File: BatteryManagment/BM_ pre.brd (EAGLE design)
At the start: 107.7 x 100 mm, 98 parts, among them IC1 LMV321M5, U1 ATMEGA328P-AU, U2 LTC4440EMS8E-5PBF

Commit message: Schematic PDF uplaod
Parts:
- moved MOTOR+ 2.20 mm to (98.3, 19.1)
- moved PAD1 1.48 mm to (35.2, 94.9)
- moved PAD2 1.47 mm to (41.4, 94.8)
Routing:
- net GND: track 58.0 -> 129.5 mm, vias 0 -> 13
- net BATTERY+: track 89.5 -> 107.1 mm
- net CHARGE_PWM: track 69.2 -> 62.3 mm
- net N$20: track 66.9 -> 65.4 mm
- net MOTOR+: track 38.3 -> 37.2 mm
- added copper zone on layer 1, net GND

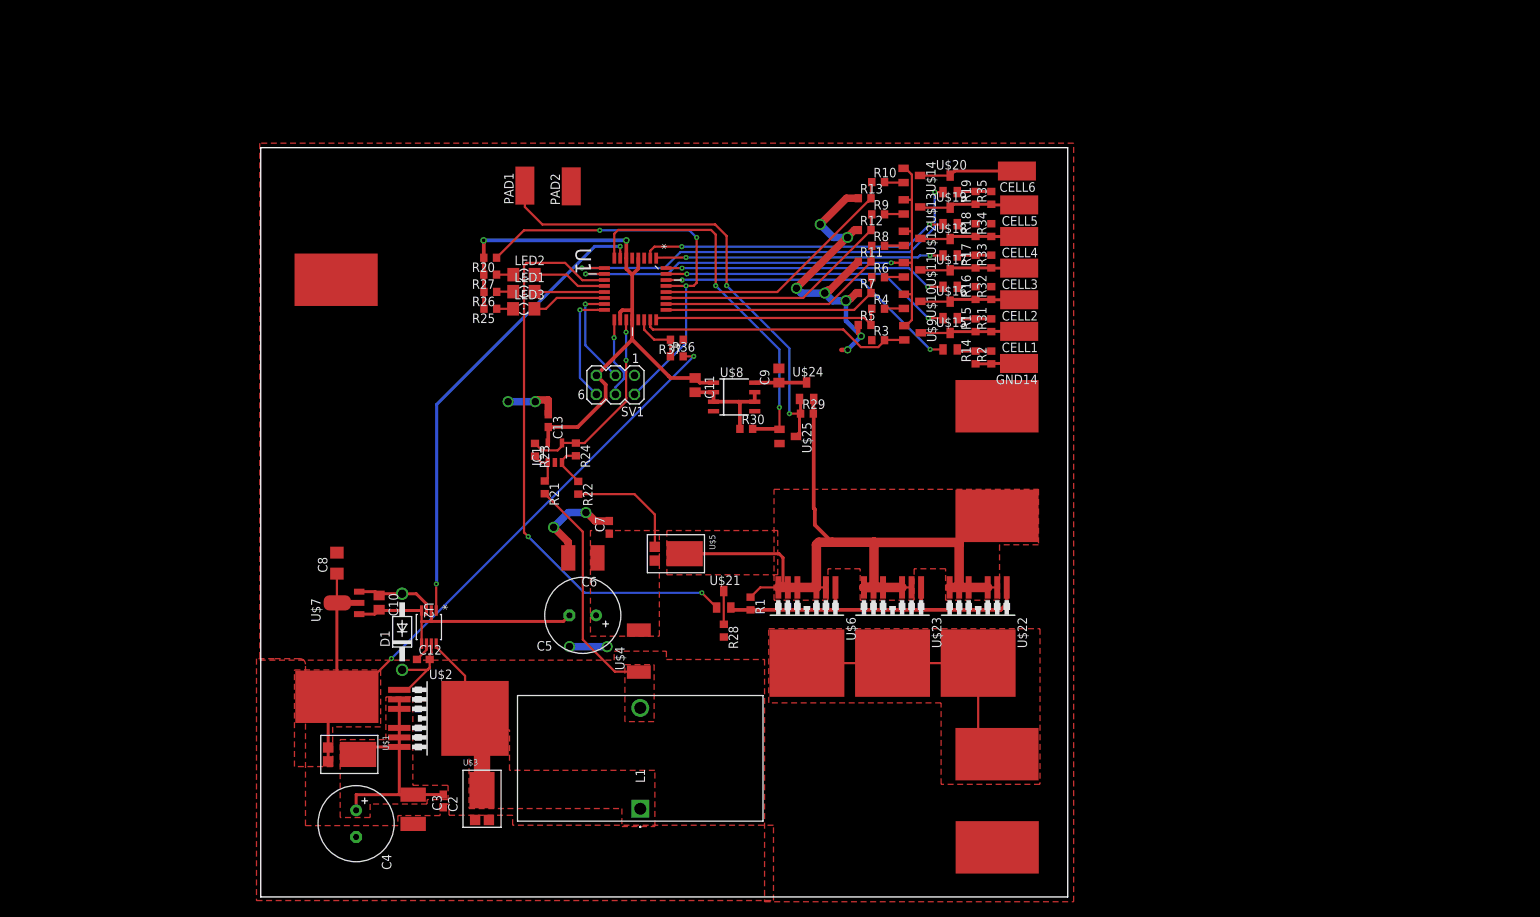
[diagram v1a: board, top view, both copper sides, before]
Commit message: just for fun.... nooot
changed some parts
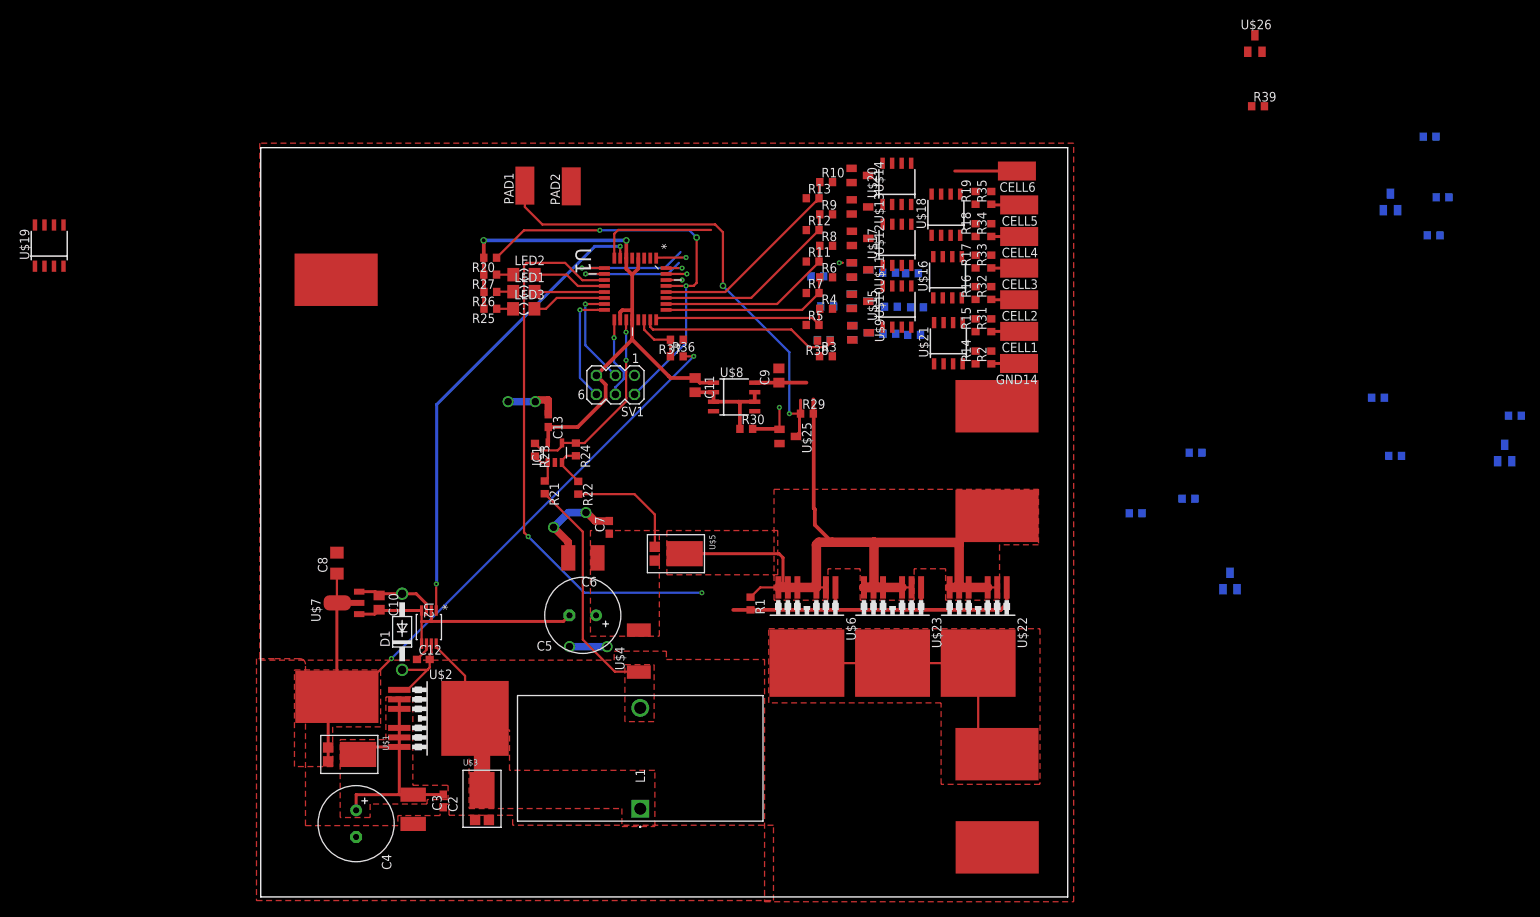
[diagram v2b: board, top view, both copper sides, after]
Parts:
- added R38, R39, R40, R41, R42, R43, R44, R45, R46, R47, R48, R49, R50, R51, R52, R53, R54, R55, R56: (no value), rcl:R0603
- added U$26, U$27, U$28, U$29, U$30, U$31: BC817, BM_pre:SOT23
- U$15, U$16, U$17, U$18, U$19, U$20, U$21: value BC817 -> IRF9310PBF; device BM_pre:SOT23 -> BM_pre:SOIC8
- U$24: value FDN306P -> BC817
- moved U$19 120.3 mm to (-28.2, 86.9)
- moved R28 46.9 mm to (87.2, 75.0), flipped to the bottom, turned to 180 degrees
- moved U$21 45.5 mm to (91.8, 73.9)
- moved U$24 10.6 mm to (80.1, 75.3), flipped to the bottom, turned to 90 degrees
- moved U$15 8.46 mm to (84.9, 78.8)
- moved U$17 8.40 mm to (84.9, 87.0)
- moved R3 7.29 mm to (75.4, 72.2)
- moved U$20 7.11 mm to (84.9, 95.2)
- moved R10 6.94 mm to (75.5, 95.4)
- moved R4 6.94 mm to (75.5, 78.5)
- moved R6 6.94 mm to (75.5, 82.7)
- moved R8 6.94 mm to (75.5, 86.9)
- moved R9 6.94 mm to (75.5, 91.1)
- moved U$10 6.94 mm to (80.0, 79.5)
- moved U$11 6.94 mm to (80.0, 83.7)
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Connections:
- new net N$21: U$10.2, U$11.2, U$12.2, U$13.2, U$14.2, U$9.2
- new net N$22: R28.1, R45.2, U$21.4
- new net N$28: R40.1, R46.2, U$15.4
- new net N$29: R41.1, R47.2, U$16.4
- new net N$3: R13.1, U$14.3
- new net N$30: R42.1, R48.2, U$17.4
- new net N$31: R43.1, R49.2, U$18.4
- new net N$32: R44.1, R50.2, U$20.4
- new net N$33: R49.1, U$28.3
- new net N$34: R50.1, U$31.3
- new net N$35: R48.1, U$29.3
- new net N$36: R47.1, U$27.3
- new net N$37: R46.1, U$30.3
- new net N$38: R45.1, U$24.3
- new net N$39: R51.2, U$31.1
- new net N$40: R52.2, U$28.1
- new net N$41: R53.2, U$29.1
- new net N$42: R54.2, U$27.1
- new net N$43: R55.2, U$30.1
- new net N$44: R56.2, U$24.1
- net ADC_BAT_1: now also R38.1; no longer U$9.2
- net BATTERY+: now also U$19.1, U$19.2, U$19.3; no longer U$24.2
- net C1_B: now also R56.1; no longer U$15.1
- net C2_B: now also R55.1; no longer U$16.1
- net C3_B: now also R54.1; no longer U$17.1
- net C4_B: now also R53.1; no longer U$18.1
- net C5_B: now also R52.1; no longer U$19.1
- net C6_B: now also R51.1; no longer U$20.1
- net CELL1: now also R28.2, R38.2, U$21.5, U$21.6, U$21.7, U$21.8; no longer U$15.3, U$9.3
- net CELL2: now also R16.2, R32.2, R4.2, R40.2, U$15.5, U$15.6, U$15.7, U$15.8; no longer R16.1, R32.1, U$10.3, U$16.3
- net CELL3: now also R17.2, R33.2, R41.2, R6.2, U$16.5, U$16.6, U$16.7, U$16.8; no longer R17.1, R33.1, U$11.3, U$17.3
- net CELL4: now also R18.2, R34.2, R42.2, R8.2, U$17.5, U$17.6, U$17.7, U$17.8; no longer R18.1, R34.1, U$12.3, U$18.3
- net CELL5: now also R19.2, R35.2, R43.2, R9.2, U$18.5, U$18.6, U$18.7, U$18.8; no longer R19.1, R35.1, U$13.3, U$19.3
- net CELL6: now also R10.2, R44.2, U$20.5, U$20.6, U$20.7, U$20.8; no longer U$14.3, U$20.3
- net CHARGE_CONTROL: now also U$26.1
- net GND: now also R39.2, U$24.2, U$27.2, U$28.2, U$29.2, U$30.2, U$31.2; no longer R11.1, R12.1, R13.1, R28.2, R3.1, R5.1, R7.1
- net MOTOR_CONTROL: now also U$26.3; no longer U$21.2
- net N$10: now also R3.1, U$9.3; no longer R10.2, U$14.2
- net N$11: now also R16.1, R32.1, U$16.1, U$16.2, U$16.3; no longer R16.2, R32.2, U$17.2
- net N$12: now also R17.1, R33.1, U$17.1, U$17.2, U$17.3; no longer R17.2, R33.2, U$18.2
- net N$13: now also R18.1, R34.1, U$18.1, U$18.2, U$18.3; no longer R18.2, R34.2, U$19.2
- net N$14: now also R19.1, R35.1, U$20.1, U$20.3; no longer R19.2, R35.2
- net N$20: now also U$19.4; no longer U$24.1
- net N$26: now also R39.1, U$26.2; no longer R28.1, U$21.3
- net N$4: now also R12.1, U$13.3; no longer R4.2, U$10.2
- net N$5: now also U$21.1, U$21.2, U$21.3; no longer U$15.2
- net N$6: now also U$15.1, U$15.2, U$15.3; no longer U$16.2
- net N$7: now also R11.1, U$12.3; no longer R6.2, U$11.2
- net N$8: now also R7.1, U$11.3; no longer R8.2, U$12.2
- net N$9: now also R5.1, U$10.3; no longer R9.2, U$13.2
- net TEST: now also U$19.5, U$19.6, U$19.7, U$19.8; no longer U$24.3
- net UC_M_CONT: no longer U$21.1
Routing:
- net V_MEAS: track 72.1 -> 16.0 mm
- net GND: track 129.5 -> 78.6 mm, vias 13 -> 6
- net C5_B: track 41.5 -> 0.00 mm, vias 2 -> 0
- net C6_B: track 58.2 -> 17.1 mm, vias 2 -> 1
- net C1_B: track 40.8 -> 2.19 mm, vias 2 -> 1
- net C2_B: track 39.4 -> 2.78 mm, vias 2 -> 1
- net C3_B: track 38.0 -> 2.14 mm, vias 2 -> 1
- net C4_B: track 38.4 -> 4.02 mm, vias 2 -> 1
- net SELBSTERHALTUNG: track 50.4 -> 22.9 mm, vias 2 -> 1
- net CELL2: track 14.7 -> 3.67 mm
- net CELL5: track 13.5 -> 3.63 mm
- net ADC_BAT_1: track 36.4 -> 26.7 mm
- net CELL3: track 13.4 -> 3.69 mm
- net CELL4: track 13.4 -> 3.71 mm
- net CELL1: track 13.2 -> 3.69 mm
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
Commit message: V0.1 finished
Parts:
- U$15, U$16, U$17, U$18, U$20, U$21: value IRF9310PBF -> BC327; device BM_pre:SOIC8 -> BM_pre:Z03A
- moved U$19 103.9 mm to (74.0, 68.3), turned to 90 degrees
- moved U$26 102.8 mm to (61.9, 39.4), turned to 180 degrees
- moved R39 99.5 mm to (58.5, 39.6), turned to 270 degrees
- moved U$31 93.7 mm to (79.9, 96.3), turned to 90 degrees
- moved R51 86.4 mm to (73.0, 95.3), turned to 180 degrees
- moved R44 86.4 mm to (87.5, 97.3), turned to 90 degrees
- moved R52 83.5 mm to (73.0, 91.0), turned to 180 degrees
- moved R49 72.8 mm to (85.0, 92.2), turned to 180 degrees
- moved U$28 70.8 mm to (80.0, 92.1), turned to 90 degrees
- moved R50 70.8 mm to (85.0, 96.5), turned to 180 degrees
- moved R43 69.0 mm to (87.5, 93.0), turned to 90 degrees
- moved U$29 67.3 mm to (80.0, 87.9), turned to 90 degrees
- moved R53 56.4 mm to (73.0, 86.8), turned to 180 degrees
- moved R48 51.8 mm to (85.0, 87.4), turned to 180 degrees
- moved R42 47.2 mm to (87.5, 88.2), turned to 90 degrees
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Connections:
- net CELL1: now also U$15.3; no longer U$21.5, U$21.6, U$21.7, U$21.8
- net CELL2: now also U$16.3; no longer U$15.5, U$15.6, U$15.7, U$15.8
- net CELL3: now also U$17.3; no longer U$16.5, U$16.6, U$16.7, U$16.8
- net CELL4: now also U$18.3; no longer U$17.5, U$17.6, U$17.7, U$17.8
- net CELL5: now also U$20.3; no longer U$18.5, U$18.6, U$18.7, U$18.8
- net CELL6: now also U$21.3; no longer U$20.5, U$20.6, U$20.7, U$20.8
- net CHARGE_CONTROL: no longer U$26.1
- net N$11: now also U$17.1; no longer U$16.1, U$16.2, U$16.3
- net N$12: now also U$18.1; no longer U$17.1, U$17.2, U$17.3
- net N$13: now also U$20.1; no longer U$18.1, U$18.2, U$18.3
- net N$14: now also U$21.1; no longer U$20.1, U$20.2, U$20.3
- net N$22: now also U$15.2; no longer U$21.4
- net N$28: now also U$16.2; no longer U$15.4
- net N$29: now also U$17.2; no longer U$16.4
- net N$30: now also U$18.2; no longer U$17.4
- net N$31: now also U$20.2; no longer U$18.4
- net N$32: now also U$21.2; no longer U$20.4
- net N$5: now also U$15.1; no longer U$21.1, U$21.2, U$21.3
- net N$6: now also U$16.1; no longer U$15.1, U$15.2, U$15.3
- net UC_M_CONT: now also U$26.1
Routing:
- net GND: track 78.6 -> 144.7 mm, vias 6 -> 12
- net V_MEAS: track 16.0 -> 73.1 mm, vias 2 -> 4
- net SELBSTERHALTUNG: track 22.9 -> 49.8 mm, vias 1 -> 2
- net N$21: track 0.00 -> 26.3 mm
- net CELL1: track 3.69 -> 29.5 mm, vias 0 -> 1
- net CELL5: track 3.63 -> 29.3 mm, vias 0 -> 1
- net CELL2: track 3.67 -> 28.9 mm, vias 0 -> 1
- net CELL4: track 3.71 -> 28.9 mm, vias 0 -> 1
- net CELL3: track 3.69 -> 28.6 mm, vias 0 -> 1
- net C5_B: track 0.00 -> 23.7 mm, vias 0 -> 1
- net CELL6: track 8.30 -> 31.1 mm, vias 0 -> 1
- net C1_B: track 2.19 -> 21.5 mm
- net C2_B: track 2.78 -> 20.1 mm
- net C6_B: track 17.1 -> 34.0 mm
- net C3_B: track 2.14 -> 18.7 mm
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
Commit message: Revert "Revert "Finished version v0.2""
This reverts commit 5ce350199b8ee6846b212b42396474e627ee3767.
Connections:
- net CHARGE_CONTROL: no longer D1.C
- net N$2: now also D1.C
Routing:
- net CHARGE_CONTROL: track 12.0 -> 8.60 mm
- net N$2: track 2.63 -> 5.19 mm
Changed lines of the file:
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@@
 <signal name="CHARGE_CONTROL">
 <contactref element="U$2" pad="1"/>
+<wire x1="22.25" y1="30.31" x2="19.66" y2="27.72" width="0.45" layer="1"/>
+<wire x1="19.66" y1="27.72" x2="18.5725" y2="27.72" width="0.3" layer="1"/>
+<wire x1="18.5725" y1="27.72" x2="18.4925" y2="27.64" width="0.3" layer="1"/>
+<wire x1="22.55" y1="30.61" x2="22.25" y2="30.31" width="0.45" layer="1"/>
 <contactref element="U2" pad="7"/>
 <contactref element="C12" pad="2"/>
-<contactref element="D1" pad="C"/>
 <wire x1="22.765" y1="33.8102" x2="22.78" y2="33.8102" width="0.3" layer="1"/>
-<wire x1="22.78" y1="32.63" x2="22.55" y2="32.4" width="0.3" layer="1"/>
-<wire x1="22.55" y1="32.4" x2="22.55" y2="31.7" width="0.3" layer="1"/>
-<wire x1="22.78" y1="33.8102" x2="22.78" y2="32.63" width="0.3" layer="1"/>
-<wire x1="22.55" y1="30.61" x2="22.55" y2="31.7" width="0.3" layer="1"/>
-<wire x1="22.25" y1="30.31" x2="19.66" y2="27.72" width="0.3" layer="1"/>
-<wire x1="19.66" y1="27.72" x2="18.5725" y2="27.72" width="0.3" layer="1"/>
-<wire x1="18.5725" y1="27.72" x2="18.4925" y2="27.64" width="0.3" layer="1"/>
-<wire x1="18.87" y1="30.31" x2="22.25" y2="30.31" width="0.3" layer="1"/>
-<wire x1="22.25" y1="30.31" x2="22.55" y2="30.61" width="0.3" layer="1"/>
+<wire x1="22.78" y1="32.63" x2="22.55" y2="32.4" width="0.45" layer="1"/>
+<wire x1="22.55" y1="32.4" x2="22.55" y2="31.7" width="0.45" layer="1"/>
+<wire x1="22.78" y1="33.8102" x2="22.78" y2="32.63" width="0.45" layer="1"/>
+<wire x1="22.55" y1="31.7" x2="22.55" y2="30.61" width="0.45" layer="1"/>
 </signal>
 <signal name="MOTOR_CONTROL">
@@
 <wire x1="22.115" y1="33.8102" x2="22.115" y2="32.965" width="0.3" layer="1"/>
 <wire x1="22.115" y1="32.965" x2="20.85" y2="31.7" width="0.3" layer="1"/>
+<contactref element="D1" pad="C"/>
+<wire x1="20.85" y1="31.7" x2="19.46" y2="30.31" width="0.3" layer="1"/>
+<wire x1="19.46" y1="30.31" x2="18.87" y2="30.31" width="0.3" layer="1"/>
 </signal>
 <signal name="N$17">

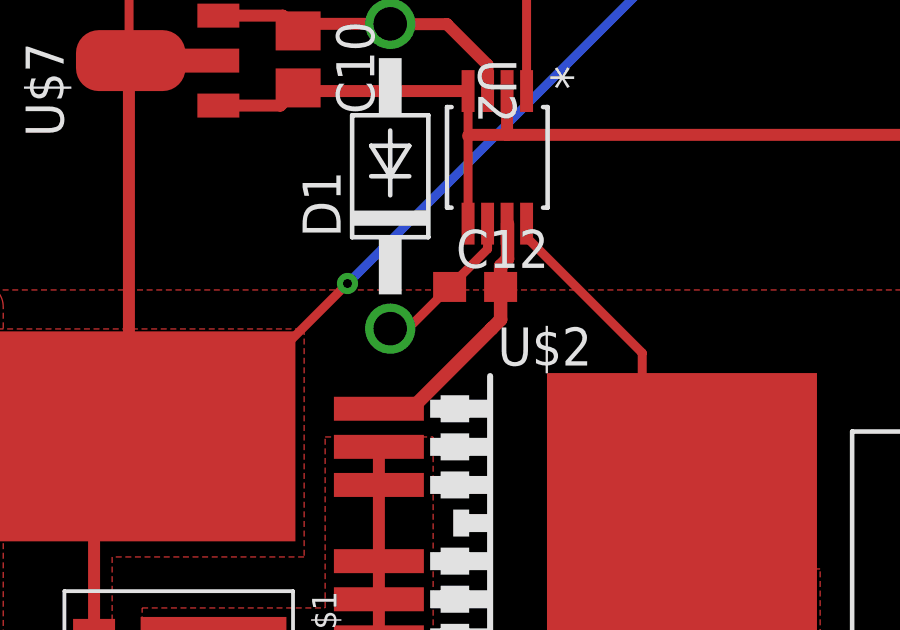
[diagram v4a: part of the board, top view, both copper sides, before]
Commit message: Revert "Finished version v0.2"
This reverts commit a5989fd47d9f9b1588f2c3c09283aac7458017f8.
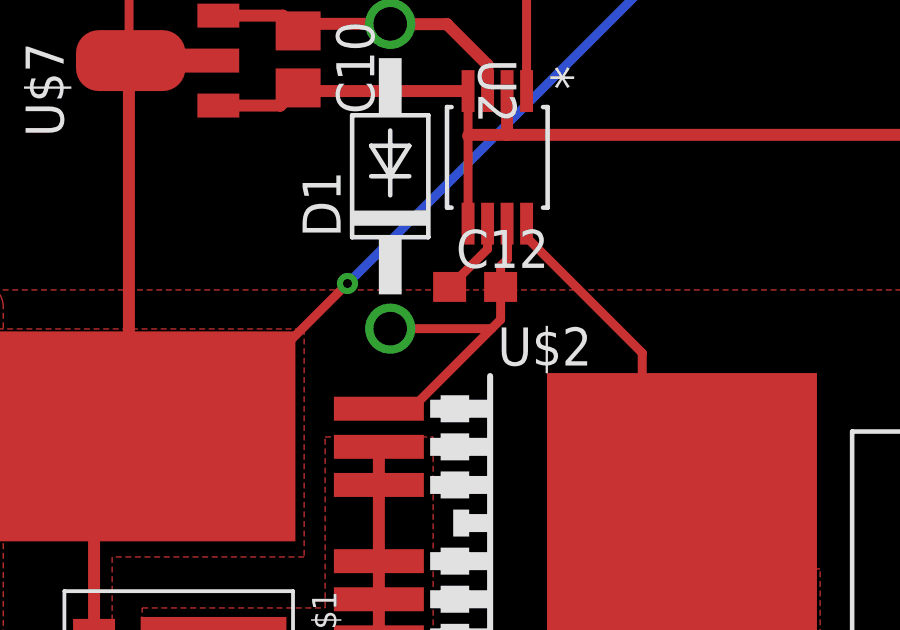
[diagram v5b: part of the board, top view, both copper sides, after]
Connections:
- net CHARGE_CONTROL: now also D1.C
- net N$2: no longer D1.C
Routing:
- net CHARGE_CONTROL: track 8.60 -> 12.0 mm
- net N$2: track 5.19 -> 2.63 mm
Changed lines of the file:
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@@
 <signal name="CHARGE_CONTROL">
 <contactref element="U$2" pad="1"/>
-<wire x1="22.25" y1="30.31" x2="19.66" y2="27.72" width="0.45" layer="1"/>
+<contactref element="U2" pad="7"/>
+<contactref element="C12" pad="2"/>
+<contactref element="D1" pad="C"/>
+<wire x1="22.765" y1="33.8102" x2="22.78" y2="33.8102" width="0.3" layer="1"/>
+<wire x1="22.78" y1="32.63" x2="22.55" y2="32.4" width="0.3" layer="1"/>
+<wire x1="22.55" y1="32.4" x2="22.55" y2="31.7" width="0.3" layer="1"/>
+<wire x1="22.78" y1="33.8102" x2="22.78" y2="32.63" width="0.3" layer="1"/>
+<wire x1="22.55" y1="30.61" x2="22.55" y2="31.7" width="0.3" layer="1"/>
+<wire x1="22.25" y1="30.31" x2="19.66" y2="27.72" width="0.3" layer="1"/>
 <wire x1="19.66" y1="27.72" x2="18.5725" y2="27.72" width="0.3" layer="1"/>
 <wire x1="18.5725" y1="27.72" x2="18.4925" y2="27.64" width="0.3" layer="1"/>
-<wire x1="22.55" y1="30.61" x2="22.25" y2="30.31" width="0.45" layer="1"/>
-<contactref element="U2" pad="7"/>
-<contactref element="C12" pad="2"/>
-<wire x1="22.765" y1="33.8102" x2="22.78" y2="33.8102" width="0.3" layer="1"/>
-<wire x1="22.78" y1="32.63" x2="22.55" y2="32.4" width="0.45" layer="1"/>
-<wire x1="22.55" y1="32.4" x2="22.55" y2="31.7" width="0.45" layer="1"/>
-<wire x1="22.78" y1="33.8102" x2="22.78" y2="32.63" width="0.45" layer="1"/>
-<wire x1="22.55" y1="31.7" x2="22.55" y2="30.61" width="0.45" layer="1"/>
+<wire x1="18.87" y1="30.31" x2="22.25" y2="30.31" width="0.3" layer="1"/>
+<wire x1="22.25" y1="30.31" x2="22.55" y2="30.61" width="0.3" layer="1"/>
 </signal>
 <signal name="MOTOR_CONTROL">
@@
 <wire x1="22.115" y1="33.8102" x2="22.115" y2="32.965" width="0.3" layer="1"/>
 <wire x1="22.115" y1="32.965" x2="20.85" y2="31.7" width="0.3" layer="1"/>
-<contactref element="D1" pad="C"/>
-<wire x1="20.85" y1="31.7" x2="19.46" y2="30.31" width="0.3" layer="1"/>
-<wire x1="19.46" y1="30.31" x2="18.87" y2="30.31" width="0.3" layer="1"/>
 </signal>
 <signal name="N$17">
